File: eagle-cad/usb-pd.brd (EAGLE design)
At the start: 68.6 x 53.3 mm, 44 parts, among them Q1 CERAMIC_RESONATOR_SMD6M00G53Z, Q2 NDS351N, U1 ATMEGA328-AU

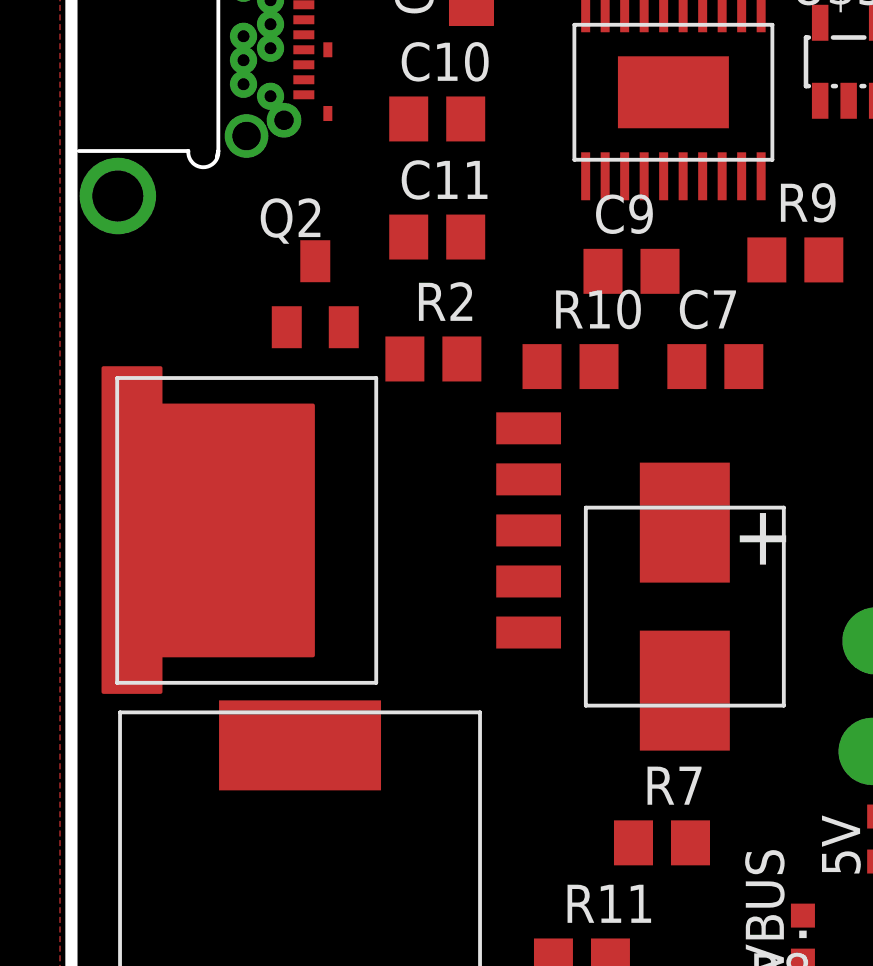
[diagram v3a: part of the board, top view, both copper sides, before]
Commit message: switched to p-channel because I'm dumb
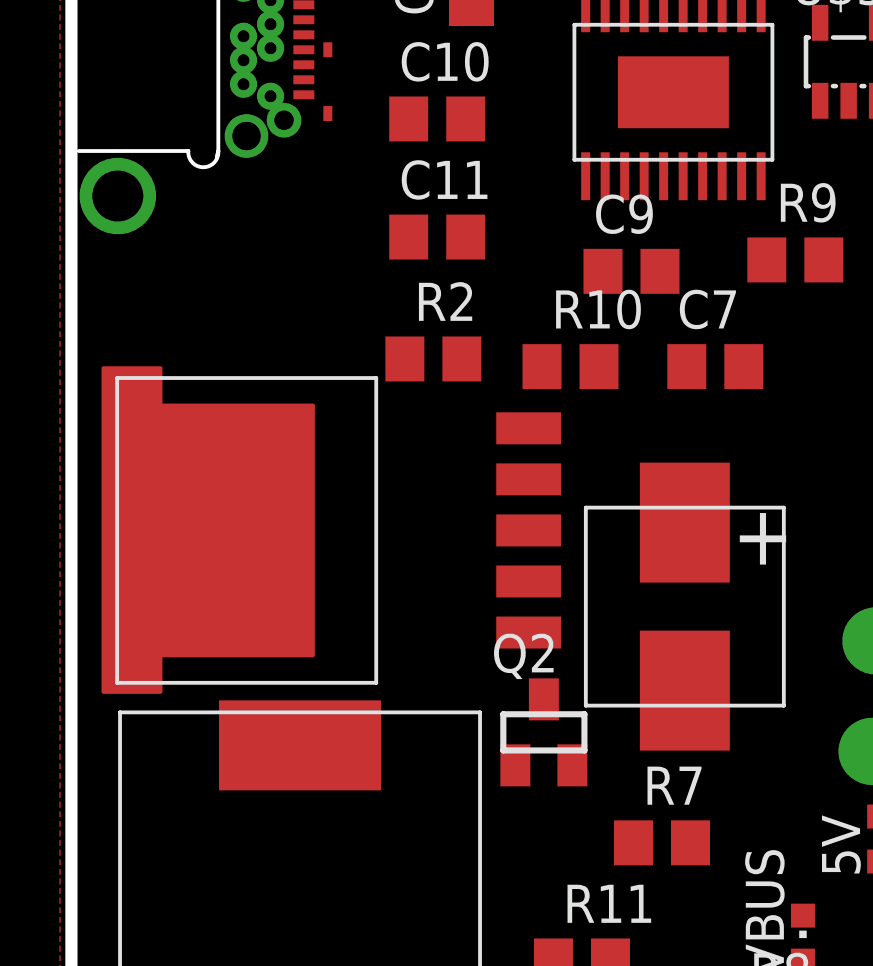
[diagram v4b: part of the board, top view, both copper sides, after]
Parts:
- Q2: value NDS351N -> FDN352A; device transistor-small-signal:SOT23 -> transistor-power:SUPER-SOT3
- moved Q2 16.5 mm to (15.7, 13.0)
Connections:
- net N$1: now also Q2.3; no longer Q2.2
- net N$40: no longer R8.2
- net VBUS: now also Q2.2, R8.2; no longer Q2.3
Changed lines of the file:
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@@
 <element name="C13" library="usb-pd" package="AVE108M10G" value="AVE108M10G24T-F" x="40.64" y="26.67"/>
 <element name="U$8" library="usb-pd" package="UWT1V101MCL1GS" value="UWT1V101MCL1GS" x="20.447" y="17.145"/>
-<element name="Q2" library="transistor-small-signal" package="SOT23" value="NDS351N" x="8.128" y="27.559"/>
 <element name="R11" library="rcl" package="R0805" value="10k" x="17.018" y="5.334"/>
+<element name="Q2" library="transistor-power" package="SUPER-SOT3" value="FDN352A" x="15.748" y="12.954"/>
 </elements>
 <signals>
@@
 <wire x1="27.813" y1="12.319" x2="32.192" y2="22.225" width="0" layer="19" extent="1-1"/>
 <wire x1="20.635" y1="9.271" x2="27.813" y2="12.319" width="0" layer="19" extent="1-1"/>
+<wire x1="17.968" y1="5.334" x2="20.635" y2="9.271" width="0" layer="19" extent="1-1"/>
 <wire x1="38.1" y1="2.54" x2="27.813" y2="12.319" width="0" layer="19" extent="1-1"/>
-<wire x1="17.968" y1="5.334" x2="20.635" y2="9.271" width="0" layer="19" extent="1-1"/>
 </signal>
 <signal name="GND">
@@
 <contactref element="C13" pad="P$2"/>
 <contactref element="U$8" pad="P$2"/>
-<wire x1="56.703" y1="34.925" x2="60.706" y2="41.656" width="0" layer="19" extent="1-1"/>
-<wire x1="57.313" y1="25.8" x2="56.703" y2="34.925" width="0" layer="19" extent="1-1"/>
-<wire x1="49.113" y1="25" x2="57.313" y2="25.8" width="0" layer="19" extent="1-1"/>
-<wire x1="44.64" y1="26.67" x2="49.113" y2="25" width="0" layer="19" extent="1-1"/>
-<wire x1="47.94" y1="17.399" x2="49.113" y2="25" width="0" layer="19" extent="1-1"/>
-<wire x1="57.719" y1="17.272" x2="57.313" y2="25.8" width="0" layer="19" extent="1-1"/>
-<wire x1="66.167" y1="25.4" x2="57.313" y2="25.8" width="0" layer="19" extent="1-1"/>
-<wire x1="43.18" y1="16.002" x2="47.94" y2="17.399" width="0" layer="19" extent="1-1"/>
-<wire x1="40.193" y1="37.846" x2="44.64" y2="26.67" width="0" layer="19" extent="1-1"/>
-<wire x1="40.64" y1="2.54" x2="43.18" y2="16.002" width="0" layer="19" extent="1-1"/>
-<wire x1="43.18" y1="2.54" x2="40.64" y2="2.54" width="0" layer="19" extent="1-1"/>
-<wire x1="31.811" y1="26.543" x2="44.64" y2="26.67" width="0" layer="19" extent="1-1"/>
-<wire x1="28.514" y1="31.877" x2="31.811" y2="26.543" width="0" layer="19" extent="1-1"/>
-<wire x1="25.908" y1="34.006" x2="28.514" y2="31.877" width="0" layer="19" extent="1-1"/>
-<wire x1="21.691" y1="31.49" x2="25.908" y2="34.006" width="0" layer="19" extent="1-1"/>
-<wire x1="19.619" y1="28.321" x2="21.691" y2="31.49" width="0" layer="19" extent="1-1"/>
-<wire x1="21.691" y1="37.09" x2="25.908" y2="34.006" width="0" layer="19" extent="1-1"/>
-<wire x1="20.32" y1="42.164" x2="21.691" y2="37.09" width="0" layer="19" extent="1-1"/>
 <wire x1="18.4277" y1="42.914" x2="20.32" y2="42.164" width="0" layer="19" extent="1-1"/>
-<wire x1="15.24" y1="23.0886" x2="19.619" y2="28.321" width="0" layer="19" extent="1-1"/>
-<wire x1="15.24" y1="19.685" x2="15.24" y2="23.0886" width="0" layer="19" extent="1-1"/>
-<wire x1="13.335" y1="39.05" x2="18.4277" y2="42.914" width="0" layer="19" extent="1-1"/>
+<wire x1="21.691" y1="37.09" x2="20.32" y2="42.164" width="0" layer="19" extent="1-1"/>
 <wire x1="10.995" y1="40.804" x2="13.335" y2="39.05" width="0" layer="19" extent="1-1"/>
 <wire x1="10.595" y1="40.804" x2="10.995" y2="40.804" width="0" layer="19" extent="1-1"/>
@@
 <wire x1="7.747" y1="39.707" x2="10.595" y2="40.804" width="0" layer="19" extent="1-1"/>
 <wire x1="6.637" y1="39.757" x2="7.747" y2="39.707" width="0" layer="19" extent="1-1"/>
-<wire x1="7.747" y1="34.207" x2="7.747" y2="39.707" width="0" layer="19" extent="1-1"/>
+<wire x1="7.747" y1="34.207" x2="13.142" y2="33.401" width="0" layer="19" extent="1-1"/>
 <wire x1="6.637" y1="34.157" x2="7.747" y2="34.207" width="0" layer="19" extent="1-1"/>
-<wire x1="13.142" y1="29.464" x2="7.747" y2="34.207" width="0" layer="19" extent="1-1"/>
-<wire x1="13.142" y1="33.401" x2="13.142" y2="29.464" width="0" layer="19" extent="1-1"/>
-<wire x1="26.416" y1="50.8" x2="20.32" y2="42.164" width="0" layer="19" extent="1-1"/>
-<wire x1="4.5466" y1="19.685" x2="15.24" y2="19.685" width="0" layer="19" extent="1-1"/>
-<wire x1="26.924" y1="10.148" x2="43.18" y2="16.002" width="0" layer="19" extent="1-1"/>
-<wire x1="24.384" y1="6.846" x2="26.924" y2="10.148" width="0" layer="19" extent="1-1"/>
-<wire x1="20.447" y1="14.345" x2="4.5466" y2="19.685" width="0" layer="19" extent="1-1"/>
 </signal>
 <signal name="AREF">
@@
 </signal>
 <signal name="N$40">
-<contactref element="R8" pad="2"/>
 <contactref element="U$2" pad="P$19"/>
 <contactref element="C10" pad="1"/>
@@
 <wire x1="17.791" y1="37.09" x2="20.391" y2="37.09" width="0" layer="19" extent="1-1"/>
 <wire x1="11.242" y1="33.401" x2="17.791" y2="37.09" width="0" layer="19" extent="1-1"/>
-<wire x1="24.191" y1="3.048" x2="11.242" y2="33.401" width="0" layer="19" extent="1-1"/>
 </signal>
 <signal name="USB-">
@@
 <contactref element="Q2" pad="1"/>
 <wire x1="56.013" y1="21.3" x2="50.8" y2="50.8" width="0" layer="19" extent="1-1"/>
-<wire x1="7.178" y1="26.459" x2="56.013" y2="21.3" width="0" layer="19" extent="1-1"/>
-<wire x1="16.068" y1="5.334" x2="7.178" y2="26.459" width="0" layer="19" extent="1-1"/>
+<wire x1="14.798" y1="11.854" x2="56.013" y2="21.3" width="0" layer="19" extent="1-1"/>
+<wire x1="16.068" y1="5.334" x2="14.798" y2="11.854" width="0" layer="19" extent="1-1"/>
 </signal>
 <signal name="IO3">
@@
 <contactref element="U$3" pad="P$4"/>
 <contactref element="POWER" pad="8"/>
-<contactref element="Q2" pad="3"/>
+<contactref element="Q2" pad="2"/>
+<contactref element="R8" pad="2"/>
 <wire x1="10.595" y1="42.254" x2="27.046" y2="46.99" width="0" layer="19" extent="1-1"/>
 <wire x1="7.747" y1="38.207" x2="10.595" y2="42.254" width="0" layer="19" extent="1-1"/>
@@
 <wire x1="6.637" y1="35.757" x2="6.637" y2="38.157" width="0" layer="19" extent="1-1"/>
 <wire x1="7.747" y1="35.707" x2="6.637" y2="35.757" width="0" layer="19" extent="1-1"/>
-<wire x1="8.128" y1="28.659" x2="7.747" y2="35.707" width="0" layer="19" extent="1-1"/>
-<wire x1="45.72" y1="2.54" x2="8.128" y2="28.659" width="0" layer="19" extent="1-1"/>
+<wire x1="16.698" y1="11.854" x2="7.747" y2="35.707" width="0" layer="19" extent="1-1"/>
+<wire x1="24.191" y1="3.048" x2="16.698" y2="11.854" width="0" layer="19" extent="1-1"/>
+<wire x1="45.72" y1="2.54" x2="24.191" y2="3.048" width="0" layer="19" extent="1-1"/>
 </signal>
 <signal name="N$1">
 <contactref element="U$6" pad="P$1"/>
 <contactref element="U$8" pad="P$1"/>
-<contactref element="Q2" pad="2"/>
+<contactref element="Q2" pad="3"/>
 <wire x1="15.24" y1="16.2814" x2="20.447" y2="19.945" width="0" layer="19" extent="1-1"/>
-<wire x1="9.078" y1="26.459" x2="15.24" y2="16.2814" width="0" layer="19" extent="1-1"/>
+<wire x1="15.748" y1="14.054" x2="15.24" y2="16.2814" width="0" layer="19" extent="1-1"/>
 </signal>
 <signal name="N$15">
@@
 <contactref element="U$7" pad="P$2"/>
 <contactref element="C13" pad="P$1"/>
-<wire x1="15.24" y1="21.3868" x2="43.053" y2="12.319" width="0" layer="19" extent="1-1"/>
+<wire x1="43.053" y1="12.319" x2="36.64" y2="26.67" width="0" layer="19" extent="1-1"/>
+<wire x1="15.24" y1="21.3868" x2="36.64" y2="26.67" width="0" layer="19" extent="1-1"/>
 <wire x1="7.62" y1="2.72" x2="15.24" y2="21.3868" width="0" layer="19" extent="1-1"/>
-<wire x1="36.64" y1="26.67" x2="7.62" y2="2.72" width="0" layer="19" extent="1-1"/>
 </signal>
 <signal name="N$9">

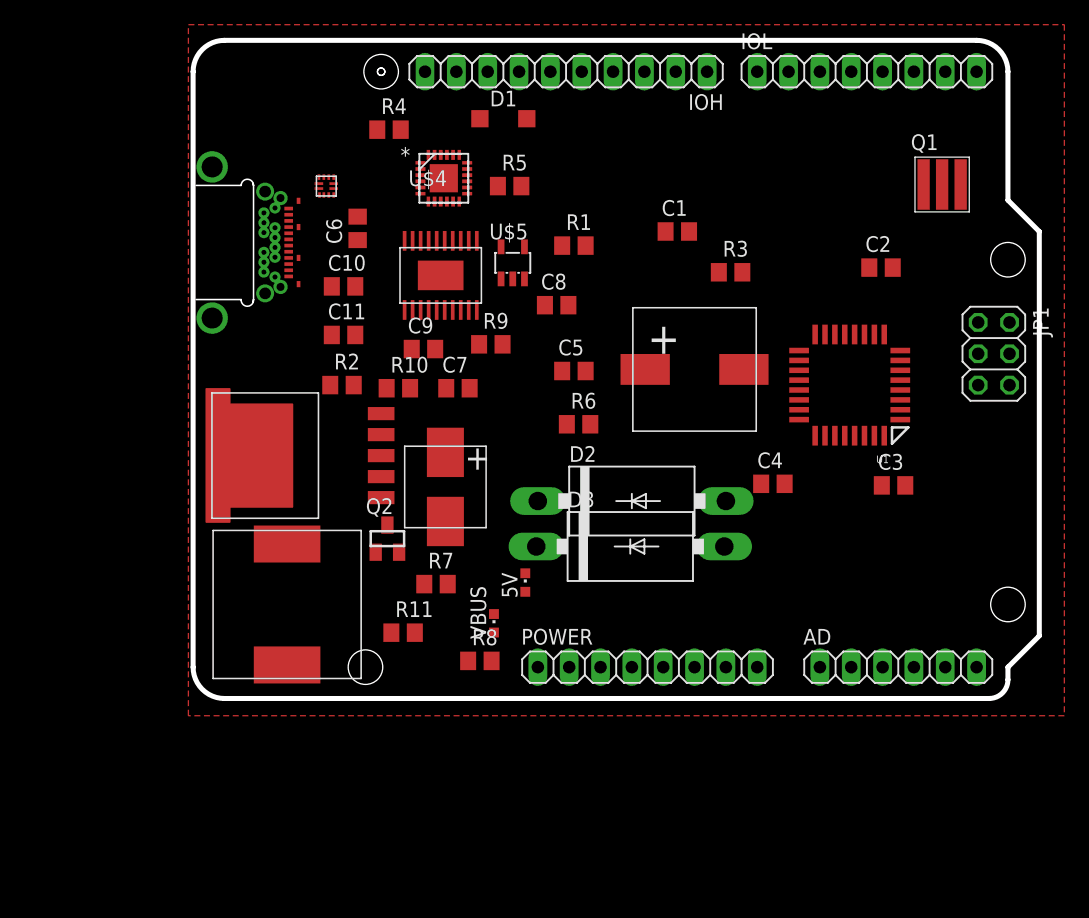
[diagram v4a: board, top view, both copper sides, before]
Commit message: Started researching proper capacitors, modified parts to have name and value on schematic
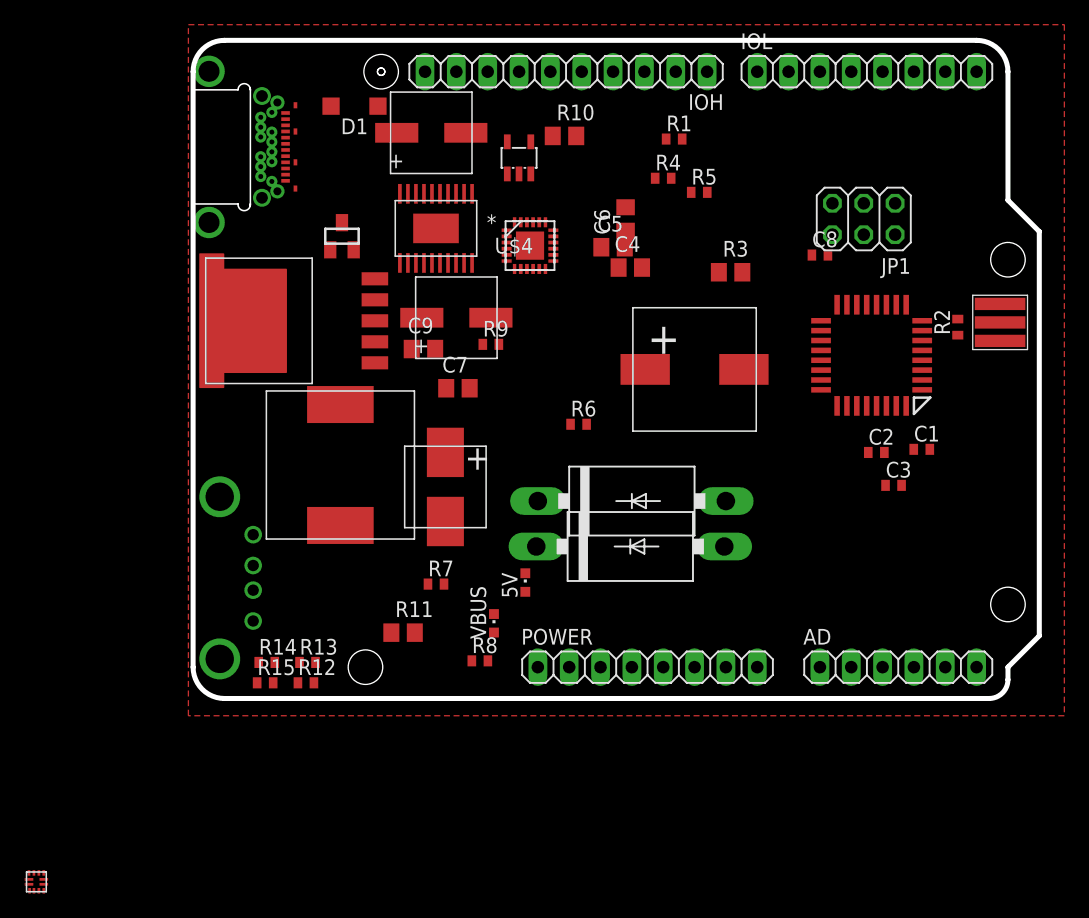
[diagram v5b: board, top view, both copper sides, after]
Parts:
- removed C10, C11: 47uF, rcl:C0805
- added R12: 43k, rcl:R0402
- added R13, R14: 51k, rcl:R0402
- added R15: 75k, rcl:R0402
- added U$10: WURTH-865080543009-47uF, usb-pd:WURTH-865090543005
- added U$11: WURTH-865090543005-22uF, usb-pd:WURTH-865090543005
- added U$9: UE27AC54100, usb-pd:UE27AC54100
- C1, C2, C3, C8: device rcl:C0805 -> rcl:C0402
- C9: value (none) -> 100n
- R1, R2, R4, R5, R6, R7, R8, R9: device rcl:R0805 -> rcl:R0402
- moved U$3 61.1 mm to (-12.7, -14.9)
- moved R2 50.1 mm to (62.0, 30.1), turned to 90 degrees
- moved C1 26.5 mm to (59.1, 20.2)
- moved Q2 24.8 mm to (12.1, 37.5)
- moved R10 24.5 mm to (30.1, 45.6)
- moved R4 22.6 mm to (38.1, 42.2)
- moved C6 21.7 mm to (35.1, 38.9)
- moved C8 21.7 mm to (50.8, 35.9)
- moved C4 21.0 mm to (35.4, 34.9)
- moved R5 15.4 mm to (41.0, 41.0)
- moved JP1 15.2 mm to (54.4, 38.9), turned to 180 degrees
- moved C2 15.0 mm to (55.4, 19.9)
- moved Q1 12.1 mm to (65.4, 30.5), turned to 270 degrees
- moved D1 12.1 mm to (13.1, 48.0), turned to 180 degrees
- moved U$7 12.1 mm to (11.9, 18.9)
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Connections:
- new net N$17: R12.1, R13.1, U$9.P$2
- new net N$18: R14.1, R15.1, U$9.P$3
- net +5V: now also R12.2, R15.2, U$11.P$1, U$9.P$1; no longer C11.1
- net GND: now also R13.2, R14.2, U$10.P$2, U$11.P$2, U$9.P$4; no longer C10.2, C11.2
- net N$40: now also U$10.P$1; no longer C10.1
